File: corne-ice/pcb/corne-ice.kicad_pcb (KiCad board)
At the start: 2 copper layers, 275.5 x 105.6 mm, 116 parts, among them J2 OLED, J4 OLED, SW1 SW_PUSH, SW10 SW_PUSH, SW11 SW_PUSH, SW12 SW_PUSH, SW13 SW_PUSH, SW14 SW_PUSH, SW15 SW_PUSH, SW16 SW_PUSH, SW17 SW_PUSH, SW18 SW_PUSH, SW19 SW_PUSH, SW2 SW_PUSH, SW20 SW_PUSH, SW21 SW_PUSH, SW22 SW_PUSH, SW23 SW_PUSH, SW24 SW_PUSH, SW25 SW_PUSH, SW26 SW_PUSH, SW27 SW_PUSH, SW28 SW_PUSH, SW29 SW_PUSH, SW3 SW_PUSH, SW30 SW_PUSH, SW31 SW_PUSH, SW32 SW_PUSH, SW33 SW_PUSH, SW34 SW_PUSH, SW35 SW_PUSH, SW36 SW_PUSH, SW37 SW_PUSH, SW38 SW_PUSH, SW39 SW_PUSH, SW4 SW_PUSH, SW40 SW_PUSH, SW41 SW_PUSH, SW42 SW_PUSH, SW5 SW_PUSH, SW6 SW_PUSH, SW7 SW_PUSH, SW8 SW_PUSH, SW9 SW_PUSH, U1 ProMicro, U2 ProMicro

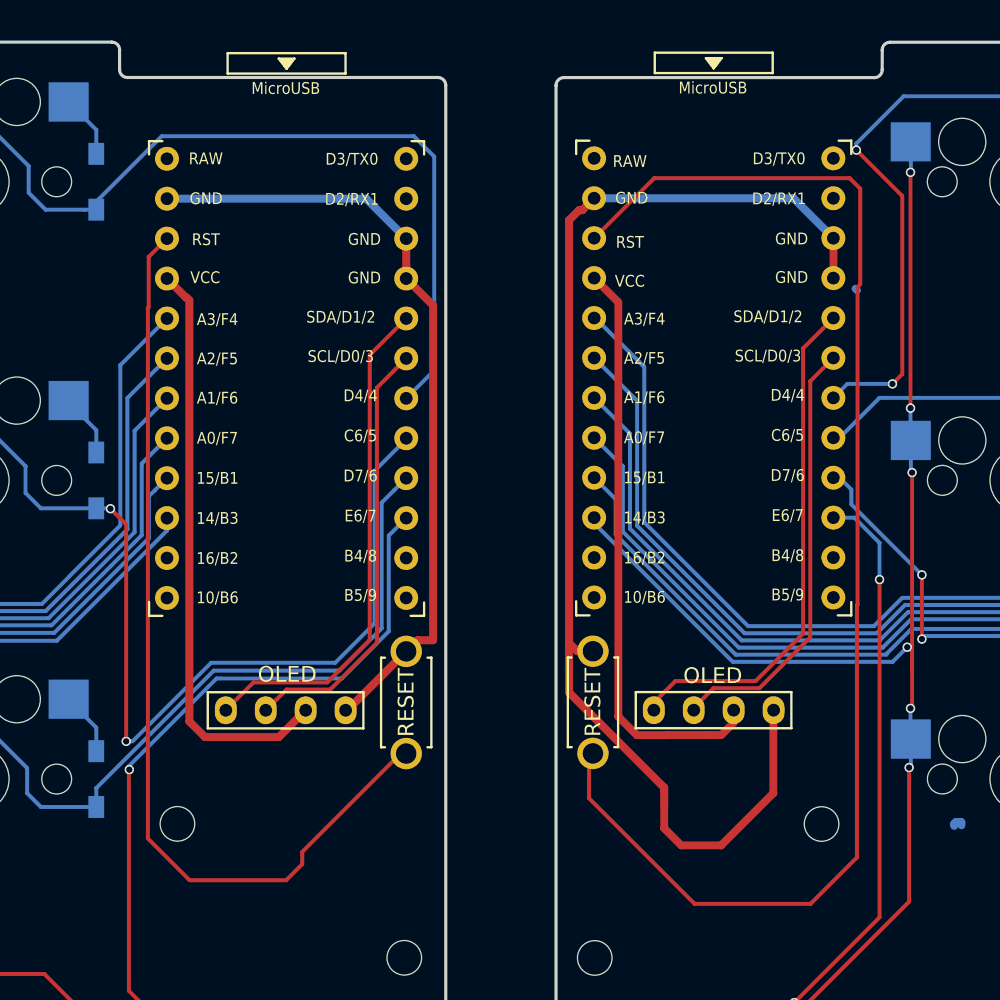
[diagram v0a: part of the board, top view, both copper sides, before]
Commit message: update oled footprint and reroute
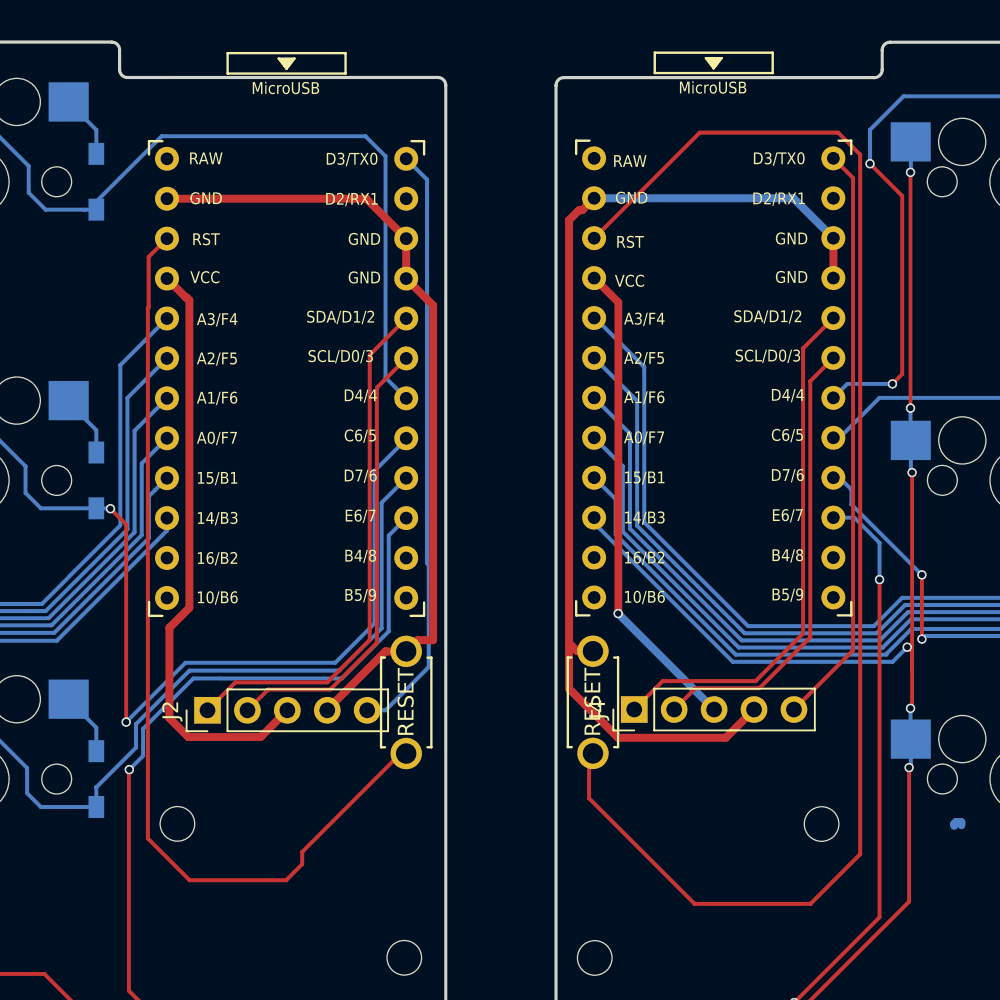
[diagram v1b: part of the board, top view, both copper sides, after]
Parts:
- J2, J4: value OLED -> nice!view; footprint kbd:OLED_1side -> Connector_PinHeader_2.54mm:PinHeader_1x05_P2.54mm_Vertical
- moved J4 1.25 mm to (156.9, 67.0), turned to 90 degrees
- moved J2 1.17 mm to (129.8, 67.0), turned to 90 degrees
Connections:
- net SCL renamed SCK
- net SCL_r renamed SCK_r
- net SDA renamed MOSI
- net SDA_r renamed MOSI_r
- U1 pad 1: LED -> CS
- U1 pad 11: Net-(U1-Pad11) -> unconnected-(U1-Pad11)
- U1 pad 12: Net-(U1-Pad12) -> unconnected-(U1-Pad12)
- U1 pad 13: Net-(U1-Pad13) -> unconnected-(U1-Pad13)
- U1 pad 14: Net-(U1-Pad14) -> unconnected-(U1-Pad14)
- U1 pad 2: data -> unconnected-(U1-Pad2)
- U1 pad 24: Net-(U1-Pad24) -> unconnected-(U1-Pad24)
- U2 pad 1: LED_r -> CS_r
- U2 pad 11: Net-(U2-Pad11) -> unconnected-(U2-Pad11)
- U2 pad 12: Net-(U2-Pad12) -> unconnected-(U2-Pad12)
- U2 pad 13: Net-(U2-Pad13) -> unconnected-(U2-Pad13)
- U2 pad 14: Net-(U2-Pad14) -> unconnected-(U2-Pad14)
- U2 pad 2: data_r -> unconnected-(U2-Pad2)
- U2 pad 24: Net-(U2-Pad24) -> unconnected-(U2-Pad24)
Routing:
- net CS: track 0.00 -> 38.0 mm
- net CS_r: track 0.00 -> 37.1 mm
- net GNDA: track 78.8 -> 67.2 mm
- net VDD: track 37.6 -> 30.6 mm, vias 0 -> 1
- net reset_r: track 85.4 -> 89.1 mm
- net row0: track 183.2 -> 179.9 mm
- net row1: track 193.2 -> 191.5 mm
- net GND: track 49.9 -> 51.1 mm
- net SCK: track 27.7 -> 28.9 mm
- net MOSI: track 32.4 -> 33.6 mm
- net SCK_r: track 27.9 -> 28.9 mm
- net row2: track 180.7 -> 181.7 mm
- net MOSI_r: track 32.7 -> 33.6 mm
- net row3: track 121.7 -> 122.5 mm
- net row0_r: track 184.4 -> 183.6 mm
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
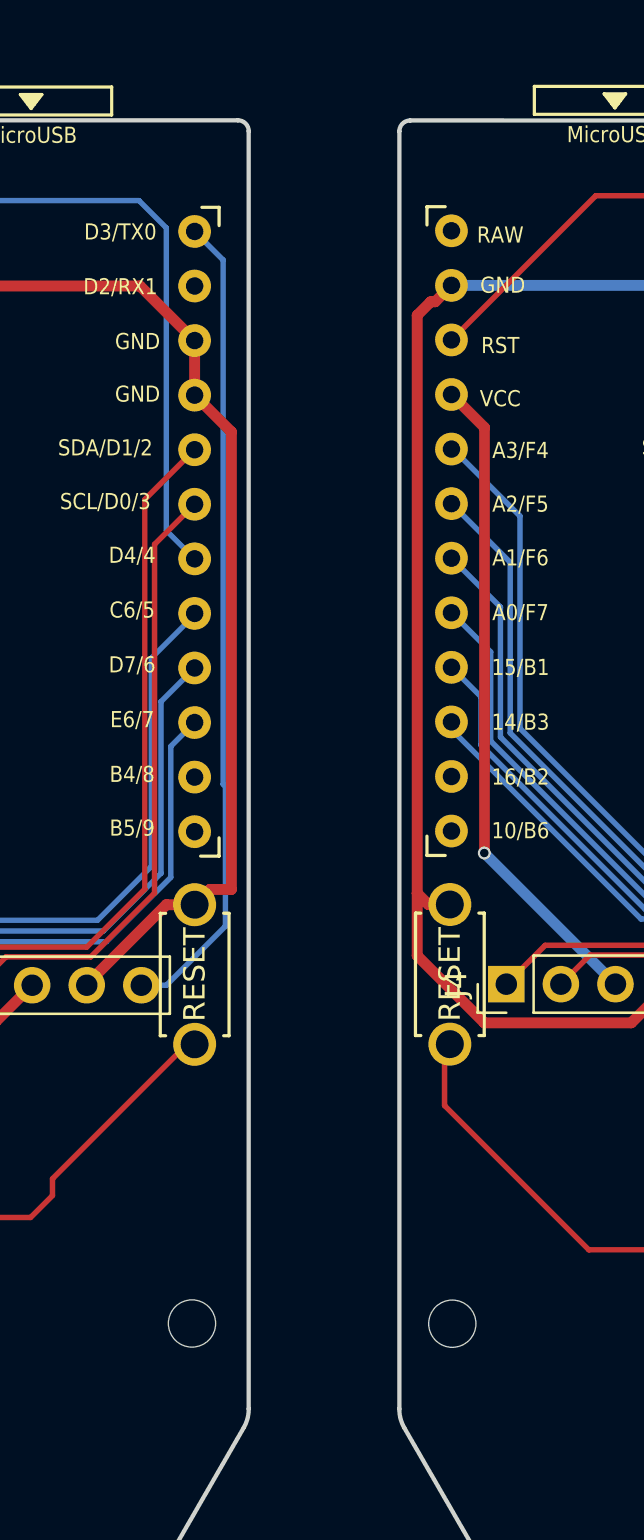
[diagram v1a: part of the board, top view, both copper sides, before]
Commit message: reset switch cutout
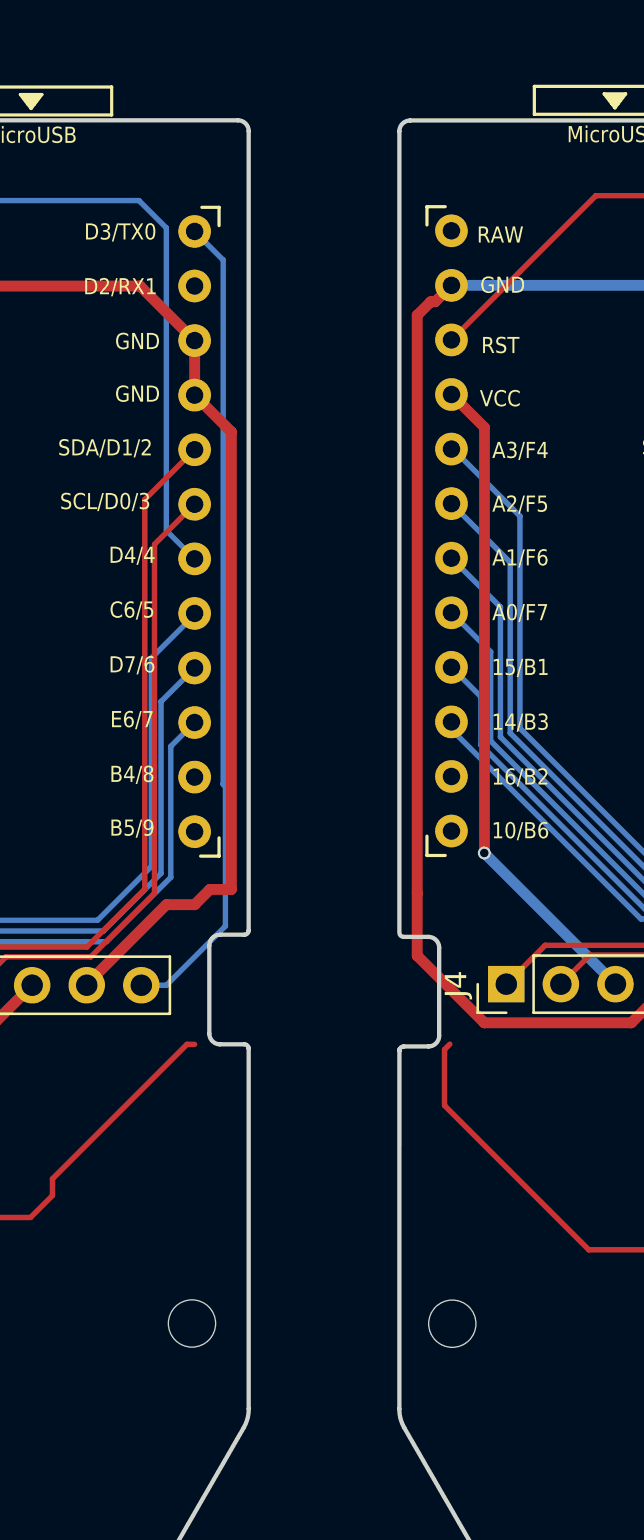
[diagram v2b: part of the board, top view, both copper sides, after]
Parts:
- removed RSW1, RSW2: SW_PUSH, kbd:ResetSW_1side
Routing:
- net GNDA: track 67.2 -> 65.5 mm
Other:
- outline, holes or cut-outs redrawn

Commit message: place remaining footprints
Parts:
- added J1: BAT, Connector_JST:JST_PH_S2B-PH-SM4-TB_1x02-1MP_P2.00mm_Horizontal, F.Cu at (139.4, 75.8)
- added J3: BAT, Connector_JST:JST_PH_S2B-PH-SM4-TB_1x02-1MP_P2.00mm_Horizontal, F.Cu at (157.5, 75.8)
- added PSW1: SW_SPDT, keeblib:switch_SSSS811101, B.Cu at (134.8, 28.6)
- added PSW2: SW_SPDT, keeblib:switch_SSSS811101, B.Cu at (162.0, 28.7)
- added RSW1: SW_PUSH, keeblib:alps_sksn, F.Cu at (144.8, 67.2)
- added RSW2: SW_PUSH, keeblib:alps_sksn, F.Cu at (152.1, 67.3)
- U1, U2: value ProMicro -> nice!nano
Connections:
- U1 pad 24: unconnected-(U1-Pad24) -> RAW
- U2 pad 24: unconnected-(U2-Pad24) -> RAW_r

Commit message: fix all routes, pass erc
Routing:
- net Net-(J3-Pad1): track 0.00 -> 68.8 mm, vias 0 -> 1
- net Net-(J1-Pad1): track 0.00 -> 66.2 mm, vias 0 -> 1
- net GND: track 51.1 -> 70.1 mm, vias 0 -> 2
- net reset_r: track 89.1 -> 73.0 mm
- net GNDA: track 65.5 -> 78.2 mm, vias 0 -> 1
- net row0: track 179.9 -> 169.1 mm
- net reset: track 60.0 -> 50.5 mm
- net RAW_r: track 0.00 -> 5.83 mm
- net RAW: track 0.00 -> 5.71 mm
- net row0_r: track 183.6 -> 180.3 mm
- net Net-(D42-Pad2): track 34.5 -> 33.7 mm
- net row3_r: track 95.3 -> 96.1 mm
- net row1_r: track 166.9 -> 166.2 mm
- net CS: track 38.0 -> 37.3 mm
- net col4_r: track 115.5 -> 114.9 mm
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
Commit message: clean up, add gerber files
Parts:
- PSW1, PSW2: value SW_SPDT -> POWER
- renumbered RSW1 to RST, RSW2 to RST
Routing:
- net row3_r: track 96.1 -> 94.7 mm
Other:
- board text added: "+ VCC"
- board text added: "- GND"
- board text added: "Corne-ice v0.1 PCB Designed by foostan/e3b0c442"
- board text added: "GND -"
- board text added: "VCC +"
- board text removed: "Corne Cherry v3.0.1 PCB Designed by foostan"
